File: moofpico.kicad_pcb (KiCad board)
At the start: 2 copper layers, 82 x 62.9 mm, 22 parts, among them J1 Conn_01x04, J100 Bus_Apple_II_Card_Side, J2 Micro_SD_Card_Det2, Q1 BS170, SW1 SW_DIP_x01, U2 74F11, U3 74LVC245, U4 74LVC245, U5 74LVC245, U6 RaspberryPi_Pico

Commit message: more gratuitous track fiddling
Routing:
- net Net-(J2-DAT3/CD): track 49.5 -> 48.3 mm
- net +3V3: track 230.5 -> 229.8 mm
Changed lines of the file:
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@@
 		(fp_arc
 			(start 10.579676 25.189937)
-			(mid 10.357949 25.493953)
+			(mid 10.357946 25.493957)
 			(end 10 25.61)
 			(stroke
@@
 	)
 	(segment
-		(start 177.786 68.17)
-		(end 179.31 68.17)
-		(width 0.254)
-		(layer "F.Cu")
-		(net 1)
-	)
-	(segment
 		(start 167.62 110.256)
 		(end 171.958 110.256)
@@
 	)
 	(segment
+		(start 177.434 67.818)
+		(end 179.31 67.818)
+		(width 0.254)
+		(layer "F.Cu")
+		(net 1)
+	)
+	(segment
 		(start 151.135 100.584)
 		(end 153.675 100.584)
@@
 	)
 	(segment
+		(start 179.31 67.818)
+		(end 179.31 62.403)
+		(width 0.254)
+		(layer "F.Cu")
+		(net 1)
+	)
+	(segment
 		(start 139.954 101.092)
 		(end 144.78 101.092)
@@
 	)
 	(segment
-		(start 176.008 66.392)
-		(end 177.786 68.17)
-		(width 0.254)
-		(layer "F.Cu")
-		(net 1)
-	)
-	(segment
 		(start 140.208 108.986)
 		(end 144.038 105.156)
@@
 	(segment
 		(start 144.78 105.156)
-		(end 144.78 94.742)
+		(end 144.78 92.964)
 		(width 0.254)
 		(layer "F.Cu")
@@
 	)
 	(segment
-		(start 179.31 68.17)
-		(end 179.31 62.403)
-		(width 0.254)
-		(layer "F.Cu")
-		(net 1)
-	)
-	(segment
 		(start 109.968 61.058)
 		(end 117.207 61.058)
@@
 	)
 	(segment
-		(start 176.008 64.491)
-		(end 176.008 66.392)
+		(start 178.998 62.091)
+		(end 178.998 60.365)
 		(width 0.254)
 		(layer "F.Cu")
@@
 	)
 	(segment
-		(start 178.998 62.091)
-		(end 178.998 60.365)
+		(start 176.008 64.491)
+		(end 176.008 66.392)
 		(width 0.254)
 		(layer "F.Cu")
@@
 	)
 	(segment
+		(start 176.008 66.392)
+		(end 177.434 67.818)
+		(width 0.254)
+		(layer "F.Cu")
+		(net 1)
+	)
+	(segment
 		(start 133.721 107.325)
 		(end 115.208 107.325)
@@
 	)
 	(segment
-		(start 144.78 92.964)
-		(end 144.78 94.742)
-		(width 0.254)
-		(layer "F.Cu")
-		(net 1)
-	)
-	(segment
 		(start 165.053 60.296)
 		(end 165.848 61.091)
@@
 	)
 	(segment
-		(start 150.368 117.348)
-		(end 149.891 117.825)
-		(width 0.127)
-		(layer "B.Cu")
-		(net 13)
-	)
-	(segment
-		(start 157.48 114.808)
-		(end 154.94 117.348)
+		(start 157.48 112.776)
+		(end 157.48 114.808)
 		(width 0.127)
 		(layer "B.Cu")
@@
 	)
 	(segment
-		(start 144.808 117.825)
+		(start 144.808 117.574)
 		(end 144.808 120.873616)
 		(width 0.127)
@@
 	)
 	(segment
-		(start 154.94 117.348)
-		(end 150.368 117.348)
+		(start 146.05 116.332)
+		(end 144.808 117.574)
 		(width 0.127)
 		(layer "B.Cu")
@@
 	)
 	(segment
-		(start 157.48 112.776)
-		(end 157.48 114.808)
+		(start 157.48 114.808)
+		(end 155.956 116.332)
 		(width 0.127)
 		(layer "B.Cu")
@@
 	)
 	(segment
-		(start 149.891 117.825)
-		(end 144.808 117.825)
+		(start 155.956 116.332)
+		(end 146.05 116.332)
 		(width 0.127)
 		(layer "B.Cu")
@@
 	)
 	(segment
-		(start 109.22 94.234)
-		(end 110.744 95.758)
+		(start 173.808 67.89)
+		(end 176.276 70.358)
 		(width 0.254)
 		(layer "F.Cu")
@@
 	)
 	(segment
-		(start 110.744 95.758)
-		(end 137.922 95.758)
+		(start 109.22 70.104)
+		(end 109.22 94.234)
 		(width 0.254)
 		(layer "F.Cu")
@@
 	)
 	(segment
-		(start 181.469 58.137)
-		(end 123.303 58.137)
+		(start 109.22 94.234)
+		(end 110.744 95.758)
 		(width 0.254)
 		(layer "F.Cu")
@@
 	)
 	(segment
-		(start 123.303 58.137)
-		(end 122.668 58.772)
+		(start 167.64 112.776)
+		(end 171.938 112.776)
 		(width 0.254)
 		(layer "F.Cu")
@@
 	)
 	(segment
-		(start 181.469 70.075)
-		(end 181.469 58.137)
+		(start 123.303 58.137)
+		(end 122.668 58.772)
 		(width 0.254)
 		(layer "F.Cu")
@@
 	)
 	(segment
-		(start 109.22 70.104)
-		(end 109.22 94.234)
+		(start 140.208 111.486)
+		(end 137.18 111.486)
 		(width 0.254)
 		(layer "F.Cu")
@@
 	)
 	(segment
-		(start 167.64 112.776)
-		(end 171.938 112.776)
+		(start 137.922 95.758)
+		(end 137.922 96.774)
 		(width 0.254)
 		(layer "F.Cu")
@@
 	)
 	(segment
-		(start 122.668 64.995)
-		(end 120.861 66.802)
+		(start 120.861 66.802)
+		(end 112.522 66.802)
 		(width 0.254)
 		(layer "F.Cu")
@@
 	)
 	(segment
-		(start 140.208 111.486)
-		(end 137.18 111.486)
+		(start 176.276 70.358)
+		(end 181.469 70.358)
 		(width 0.254)
 		(layer "F.Cu")
@@
 	)
 	(segment
-		(start 137.922 95.758)
-		(end 137.922 96.774)
+		(start 137.922 89.916)
+		(end 143.002 89.916)
 		(width 0.254)
 		(layer "F.Cu")
@@
 	)
 	(segment
-		(start 137.922 89.916)
-		(end 143.002 89.916)
+		(start 110.744 95.758)
+		(end 137.922 95.758)
 		(width 0.254)
 		(layer "F.Cu")
@@
 	)
 	(segment
-		(start 173.808 64.491)
-		(end 173.808 69.78)
+		(start 181.469 58.137)
+		(end 123.303 58.137)
 		(width 0.254)
 		(layer "F.Cu")
@@
 	)
 	(segment
-		(start 173.808 69.78)
-		(end 174.103 70.075)
+		(start 122.668 64.995)
+		(end 120.861 66.802)
 		(width 0.254)
 		(layer "F.Cu")
@@
 	)
 	(segment
-		(start 174.103 70.075)
-		(end 181.469 70.075)
+		(start 173.808 64.491)
+		(end 173.808 67.89)
 		(width 0.254)
 		(layer "F.Cu")
@@
 	)
 	(segment
-		(start 135.89 98.806)
-		(end 137.922 96.774)
+		(start 112.522 66.802)
+		(end 109.22 70.104)
 		(width 0.254)
 		(layer "F.Cu")
@@
 	)
 	(segment
-		(start 112.522 66.802)
-		(end 109.22 70.104)
+		(start 135.89 98.806)
+		(end 137.922 96.774)
 		(width 0.254)
 		(layer "F.Cu")
@@
 	)
 	(segment
-		(start 120.861 66.802)
-		(end 112.522 66.802)
+		(start 135.89 100.503)
+		(end 135.89 98.806)
 		(width 0.254)
 		(layer "F.Cu")
@@
 	)
 	(segment
-		(start 135.89 100.503)
-		(end 135.89 98.806)
+		(start 181.469 70.358)
+		(end 181.469 58.137)
 		(width 0.254)
 		(layer "F.Cu")
@@
 	)
 	(segment
-		(start 174.908 64.691)
-		(end 174.908 67.197)
+		(start 180.453 59.28)
+		(end 140.575 59.28)
 		(width 0.127)
 		(layer "F.Cu")
@@
 	)
 	(segment
-		(start 180.453 59.28)
-		(end 140.575 59.28)
+		(start 174.908 64.691)
+		(end 174.908 67.197)
 		(width 0.127)
 		(layer "F.Cu")
@@
 	)
 	(segment
-		(start 174.908 67.197)
-		(end 177.024 69.313)
+		(start 140.448 59.407)
+		(end 140.448 64.995)
 		(width 0.127)
 		(layer "F.Cu")
@@
 	)
 	(segment
-		(start 177.024 69.313)
-		(end 180.58 69.313)
+		(start 180.58 59.407)
+		(end 180.453 59.28)
 		(width 0.127)
 		(layer "F.Cu")
@@
 	)
 	(segment
-		(start 180.58 69.313)
-		(end 180.58 59.407)
+		(start 176.799 69.088)
+		(end 180.58 69.088)
 		(width 0.127)
 		(layer "F.Cu")
@@
 	)
 	(segment
-		(start 140.448 59.407)
-		(end 140.448 64.995)
+		(start 174.908 67.197)
+		(end 176.799 69.088)
 		(width 0.127)
 		(layer "F.Cu")
@@
 	)
 	(segment
-		(start 180.58 59.407)
-		(end 180.453 59.28)
+		(start 180.58 69.088)
+		(end 180.58 59.407)
 		(width 0.127)
 		(layer "F.Cu")
@@
 	)
 	(segment
-		(start 152.386 75.028)
-		(end 152.386 81.28)
-		(width 0.127)
-		(layer "F.Cu")
-		(net 36)
-	)
-	(segment
 		(start 152.386 81.28)
 		(end 160.993 81.28)
@@
 	)
 	(segment
-		(start 168.388 73.885)
-		(end 168.388 69.313)
-		(width 0.127)
-		(layer "F.Cu")
-		(net 36)
-	)
-	(segment
-		(start 160.993 81.28)
-		(end 168.388 73.885)
+		(start 171.608 67.152)
+		(end 171.608 65.091)
 		(width 0.127)
 		(layer "F.Cu")
@@
 	)
 	(segment
-		(start 168.388 69.313)
-		(end 169.404 68.297)
+		(start 145.528 68.17)
+		(end 152.386 75.028)
 		(width 0.127)
 		(layer "F.Cu")
@@
 	)
 	(segment
-		(start 171.481 68.297)
-		(end 171.608 68.17)
+		(start 152.386 75.028)
+		(end 152.386 81.28)
 		(width 0.127)
 		(layer "F.Cu")
@@
 	)
 	(segment
-		(start 145.528 68.17)
-		(end 152.386 75.028)
+		(start 166.878 75.395)
+		(end 166.878 71.882)
 		(width 0.127)
 		(layer "F.Cu")
@@
 	)
 	(segment
-		(start 171.608 68.17)
-		(end 171.608 65.091)
+		(start 145.528 64.995)
+		(end 145.528 68.17)
 		(width 0.127)
 		(layer "F.Cu")
@@
 	)
 	(segment
-		(start 169.404 68.297)
-		(end 171.481 68.297)
+		(start 166.878 71.882)
+		(end 171.608 67.152)
 		(width 0.127)
 		(layer "F.Cu")
@@
 	)
 	(segment
-		(start 145.528 64.995)
-		(end 145.528 68.17)
+		(start 160.993 81.28)
+		(end 166.878 75.395)
 		(width 0.127)
 		(layer "F.Cu")

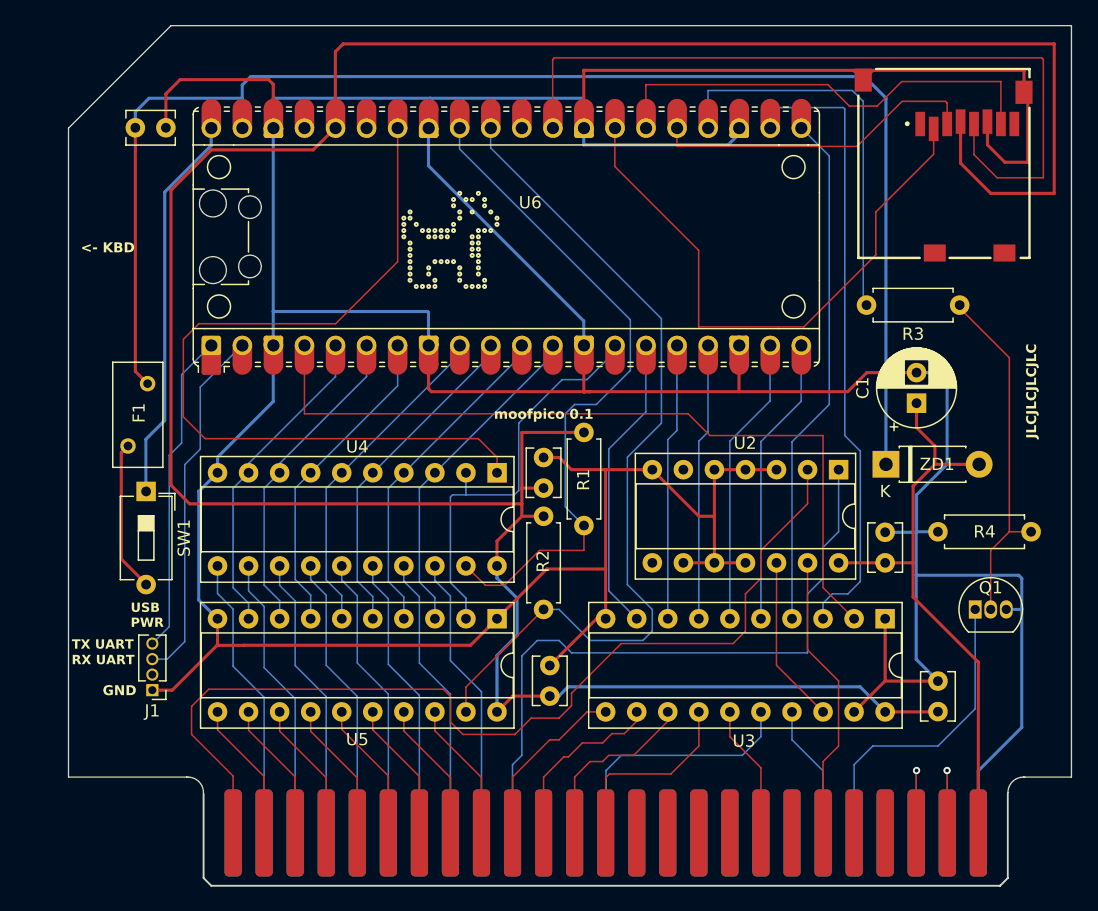
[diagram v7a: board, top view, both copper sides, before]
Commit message: major design change: get rid of the uart headers and usb power dip switch I'm not convinced they're actually needed, and the stuff around the USB power in the pico manual makes me think it's superfluous at best
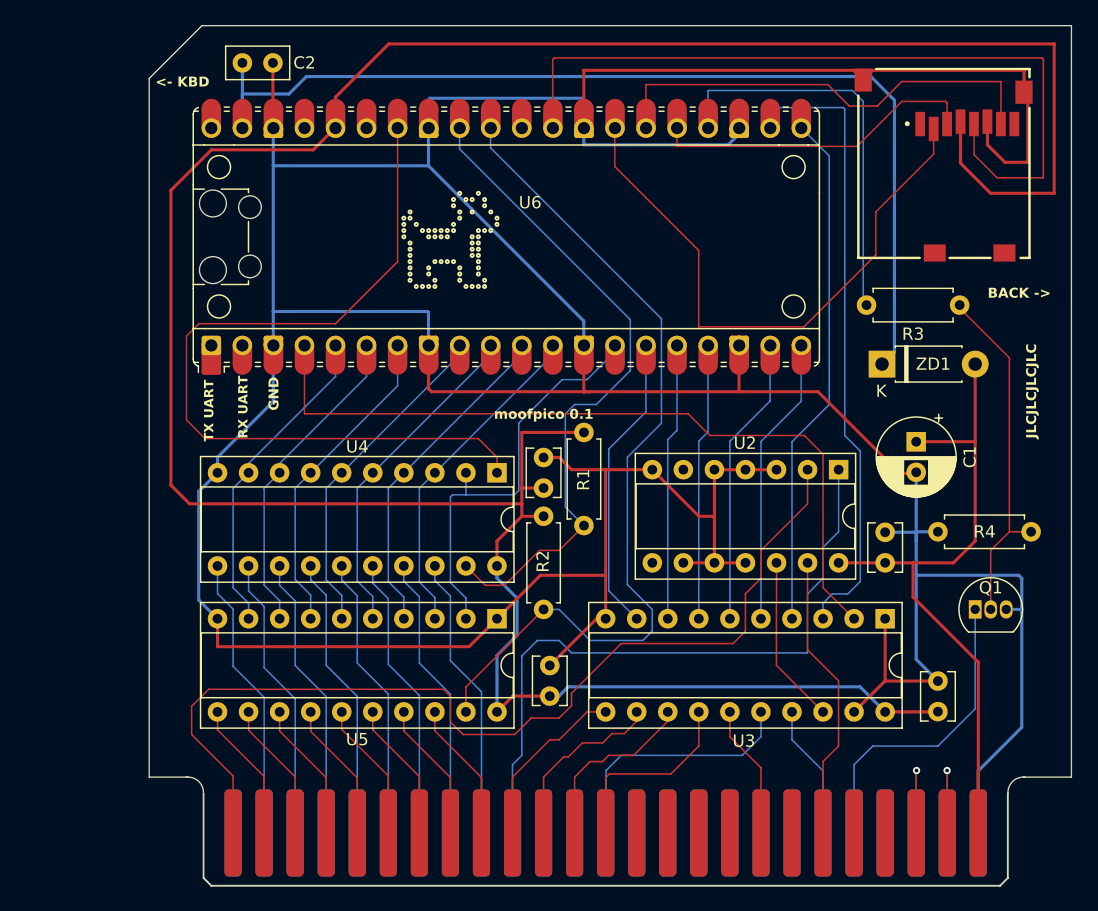
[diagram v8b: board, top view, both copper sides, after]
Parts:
- removed F1: 60R050XUL, Fuse:Fuse_BelFuse_0ZRE0005FF_L8.3mm_W3.8mm
- removed J1: Conn_01x04, Connector_PinHeader_1.27mm:PinHeader_1x04_P1.27mm_Vertical
- removed SW1: SW_DIP_x01, Button_Switch_THT:SW_DIP_SPSTx01_Slide_6.7x4.1mm_W7.62mm_P2.54mm_LowProfile
- C2: value .1u -> 22uf 10v; footprint Capacitor_THT:C_Disc_D3.8mm_W2.6mm_P2.50mm -> Capacitor_THT:C_Disc_D5.0mm_W2.5mm_P2.50mm
- moved C2 10.2 mm to (115.1, 59.7)
- moved ZD1 8.20 mm to (167.4, 84.3)
- moved C1 3.15 mm to (170.2, 90.7), turned to -90 degrees
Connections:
- U6 pad 1: Net-(J1-Pin_4) -> unconnected-(U6-GPIO0-Pad1)_0
- U6 pad 2: Net-(J1-Pin_3) -> unconnected-(U6-GPIO1-Pad2)_0
- U6 pad 40: Net-(U6-VBUS) -> unconnected-(U6-VBUS-Pad40)
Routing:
- net Net-(U6-VSYS): track 119.0 -> 84.9 mm
- net Net-(U6-VBUS): track 31.9 -> 0.00 mm
- net Net-(J1-Pin_3): track 29.4 -> 0.00 mm
- net GND: track 424.5 -> 396.2 mm
- net Net-(J1-Pin_4): track 26.4 -> 0.00 mm
- net Net-(F1-Pad1): track 12.3 -> 0.00 mm
- net +5V: track 48.4 -> 55.5 mm
- net +3V3: track 229.8 -> 227.6 mm
- net D/OE: track 55.7 -> 54.5 mm
- net ENBL: track 64.8 -> 63.9 mm
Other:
- board size 82 x 62.9 mm -> 75.4 x 62.9 mm
- board text added: "BACK ->"
- board text removed: "USB PWR"
